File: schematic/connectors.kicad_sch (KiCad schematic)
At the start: 17 parts, among them J1 Conn_01x06, J2 Conn_01x03, J3 Conn_01x03, J4 Conn_01x02

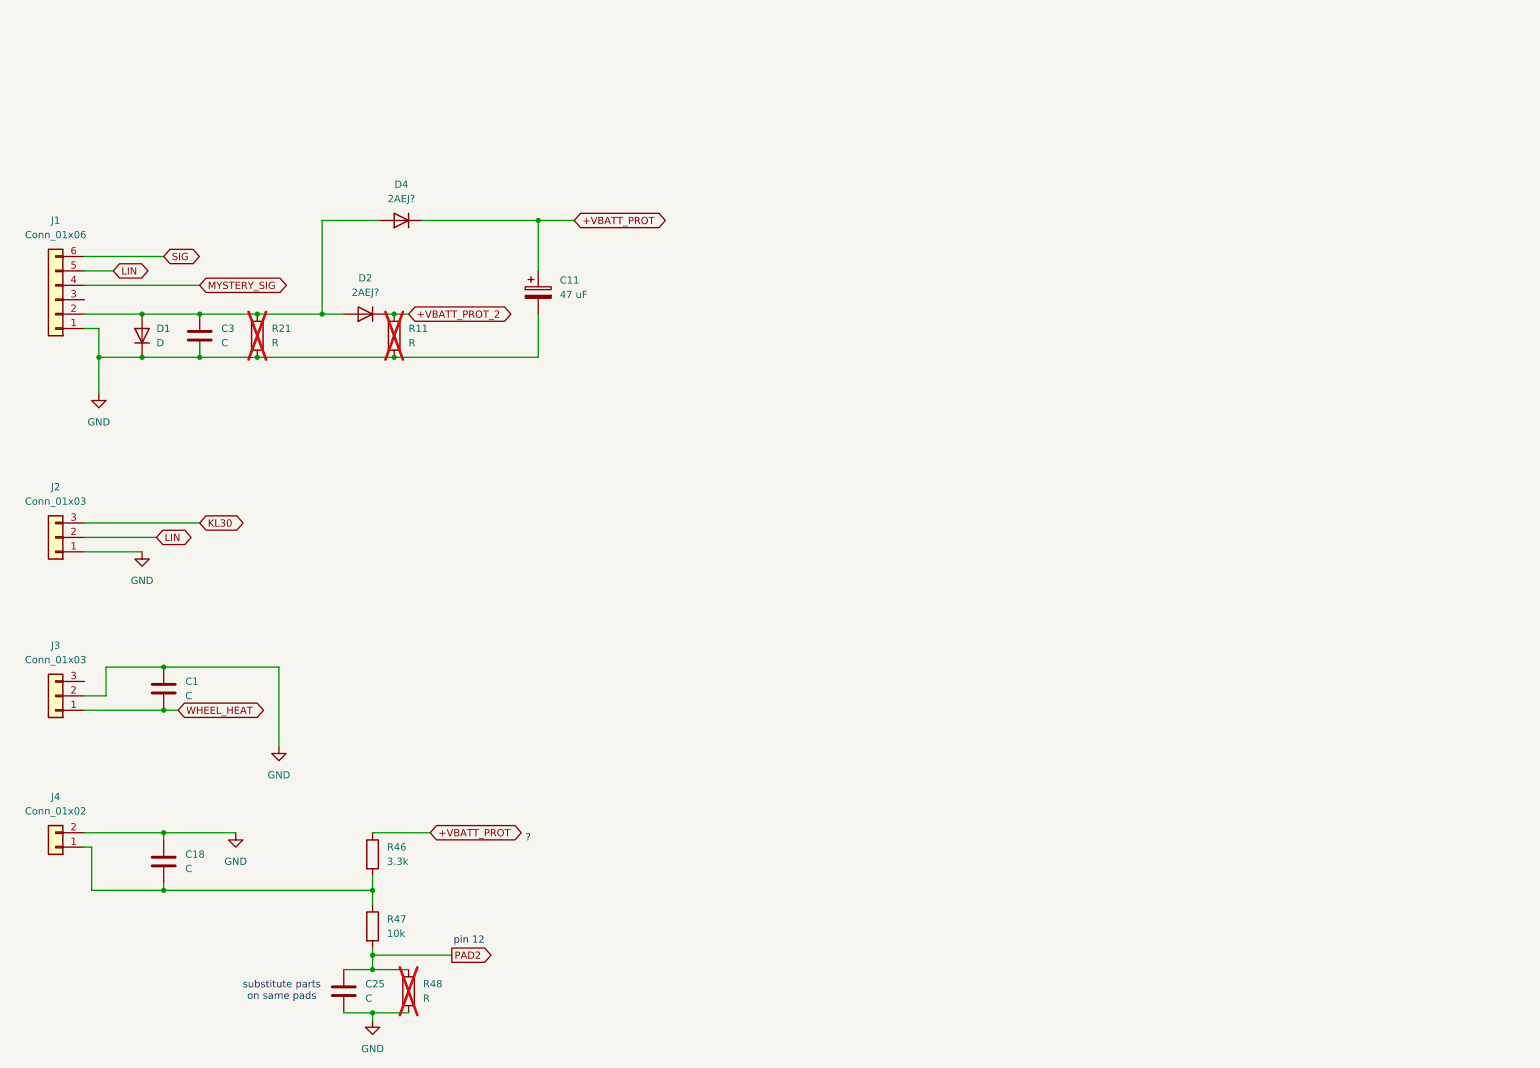
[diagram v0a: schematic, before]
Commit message: Added J5 and assoc. resistor network. Added traceable signals for MYSTERY_SIG
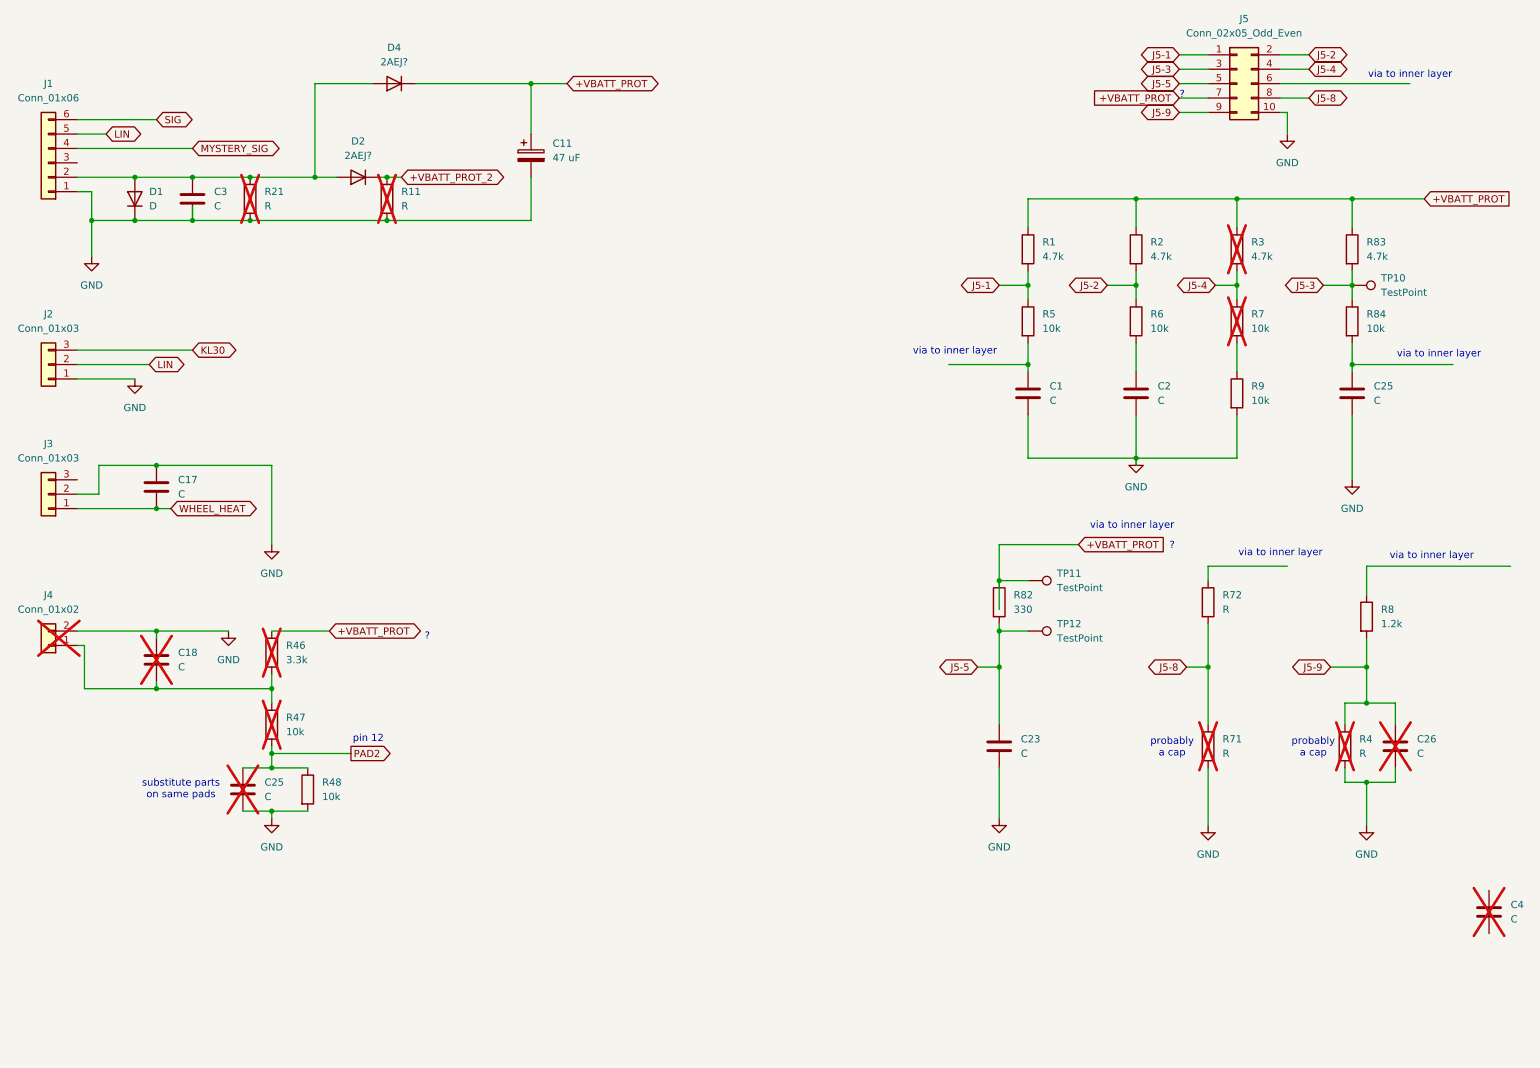
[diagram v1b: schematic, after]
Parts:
- added C1, C2, C23, C25, C26, C4: C, symbol Device:C
- added J5: Conn_02x05_Odd_Even, symbol Connector_Generic:Conn_02x05_Odd_Even
- added R1, R2, R3, R83: 4.7k, symbol Device:R
- added R4, R71, R72: R, symbol Device:R
- added R5, R6, R7, R84, R9: 10k, symbol Device:R
- added R8: 1.2k, symbol Device:R
- added R82: 330, symbol Device:R
- added TP10, TP11, TP12: TestPoint, symbol Connector:TestPoint
- C18, C25, J4, R46, R47: now not fitted
- R48: value R -> 10k; now fitted
- renumbered C1 to C17
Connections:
- net +VBATT_PROT: now also J5.7 (Pin_7), R1.1, R2.1, R3.1, R82.1, R83.1, TP11.1
- net GND: now also C1.2, C2.2, C23.2, C25.2, C26.2, J5.10 (Pin_10), R4.2, R71.2, R9.2
- new net: C25.1, R84.2
- new net: R7.2, R9.1
- new net: C2.1, R6.2
- new net: C1.1, R5.2
- new net J5-1: J5.1 (Pin_1), R1.2, R5.1
- new net J5-2: J5.2 (Pin_2), R2.2, R6.1
- new net J5-3: J5.3 (Pin_3), R83.2, R84.1, TP10.1
- new net J5-4: J5.4 (Pin_4), R3.2, R7.1
- new net J5-5: C23.1, J5.5 (Pin_5), R82.2, TP12.1
- new net J5-8: J5.8 (Pin_8), R71.1, R72.2
- new net J5-9: C26.1, J5.9 (Pin_9), R4.1, R8.2
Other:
- note added: "probably a cap"
- note added: "via to inner layer"
- moved on the sheet: C11, C17, C3, D1, D2, D4, J1, J2, J3, R11, R21
